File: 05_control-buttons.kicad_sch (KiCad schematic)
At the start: 8 parts, among them SW1 SW_Push, SW2 SW_Push, SW3 SW_Push, SW4 SW_Push

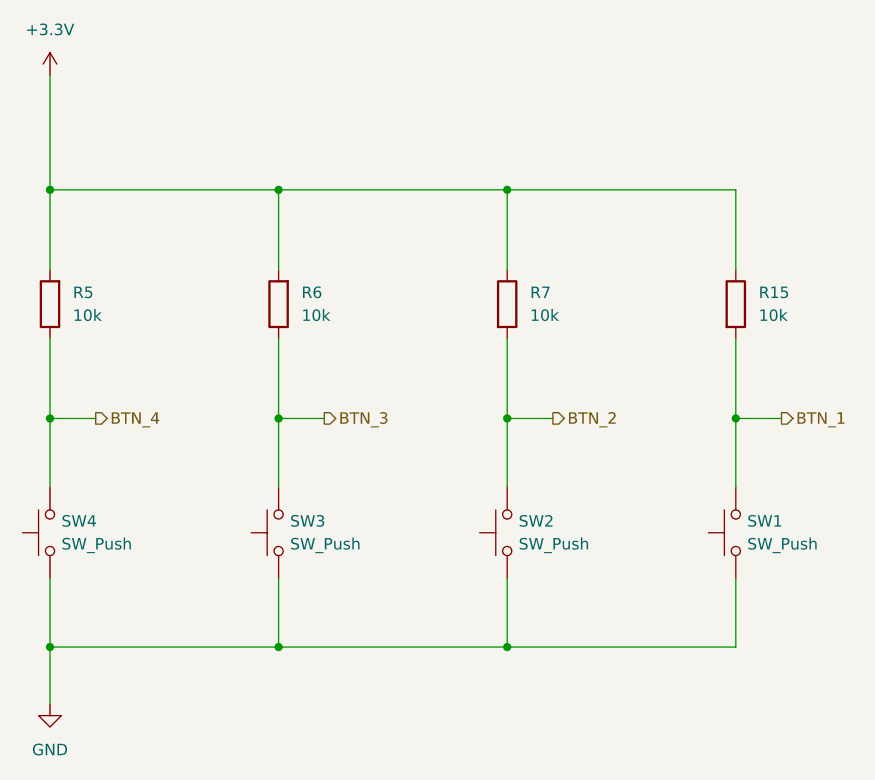
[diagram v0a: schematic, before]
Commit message: Reworked v2 routing
- some general improvements
- reworked component numbering
- routed and tuned differential pair (USB)
- added stiching vias and improved ground fills
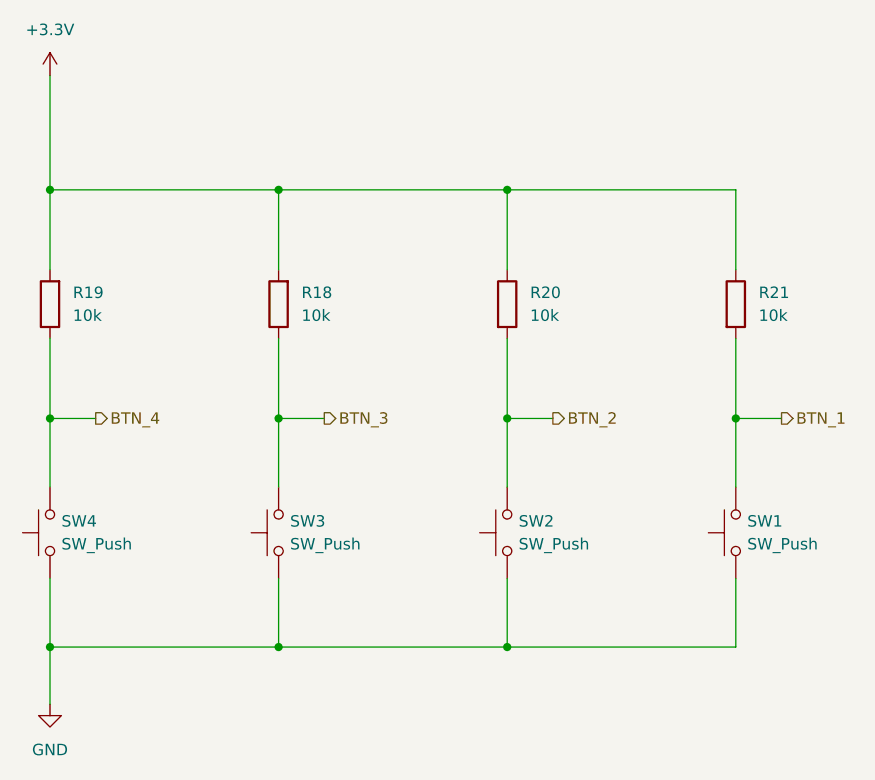
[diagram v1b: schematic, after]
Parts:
- renumbered R6 to R18, R5 to R19, R7 to R20, R15 to R21
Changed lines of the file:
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@@
 		(dnp no)
 		(fields_autoplaced yes)
-		(property "Reference" "R6"
+		(property "Reference" "R18"
 			(at 104.14 74.9299 0)
 			(effects
@@
 			(project "ZEReader-Pico"
 				(path "/ec954637-2a8b-4662-b4a1-f88107f11cb0/33ac9274-8ec9-4374-b845-560e6893b431"
-					(reference "R6")
+					(reference "R18")
 					(unit 1)
 				)
@@
 		(dnp no)
 		(fields_autoplaced yes)
-		(property "Reference" "R15"
+		(property "Reference" "R21"
 			(at 154.94 74.9299 0)
 			(effects
@@
 			(project "ZEReader-Pico"
 				(path "/ec954637-2a8b-4662-b4a1-f88107f11cb0/33ac9274-8ec9-4374-b845-560e6893b431"
-					(reference "R15")
+					(reference "R21")
 					(unit 1)
 				)
@@
 		(dnp no)
 		(fields_autoplaced yes)
-		(property "Reference" "R5"
+		(property "Reference" "R19"
 			(at 78.74 74.9299 0)
 			(effects
@@
 			(project ""
 				(path "/ec954637-2a8b-4662-b4a1-f88107f11cb0/33ac9274-8ec9-4374-b845-560e6893b431"
-					(reference "R5")
+					(reference "R19")
 					(unit 1)
 				)
@@
 		(dnp no)
 		(fields_autoplaced yes)
-		(property "Reference" "R7"
+		(property "Reference" "R20"
 			(at 129.54 74.9299 0)
 			(effects
@@
 			(project "ZEReader-Pico"
 				(path "/ec954637-2a8b-4662-b4a1-f88107f11cb0/33ac9274-8ec9-4374-b845-560e6893b431"
-					(reference "R7")
-					(unit 1)
-				)
+					(reference "R20")
+					(unit 1)
+				)

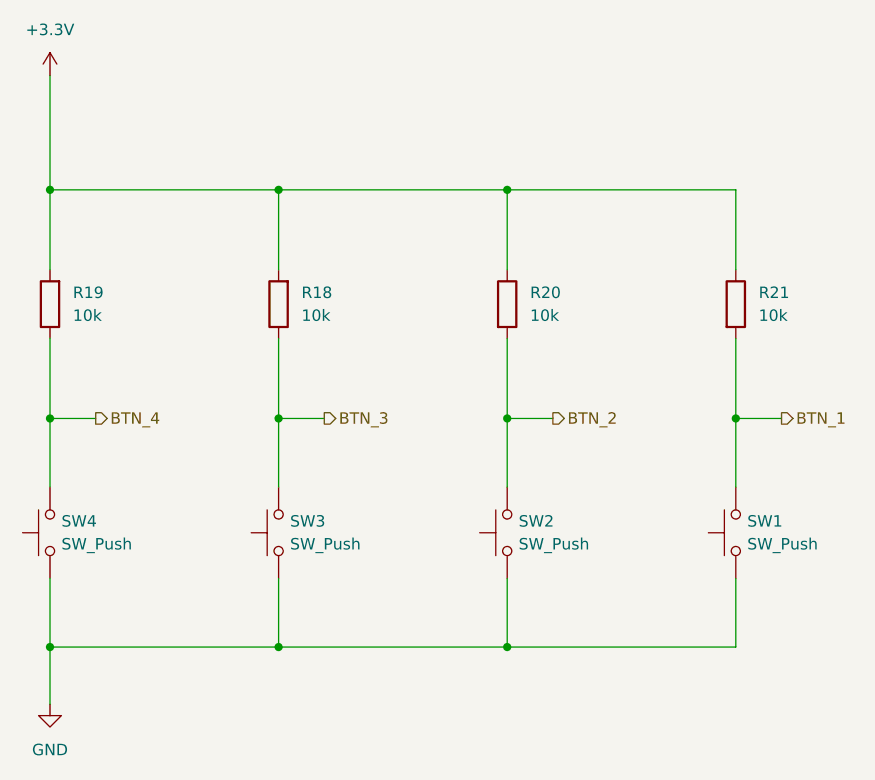
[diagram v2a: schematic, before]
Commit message: Connect both USB data lines again, checked everything with datasheets again
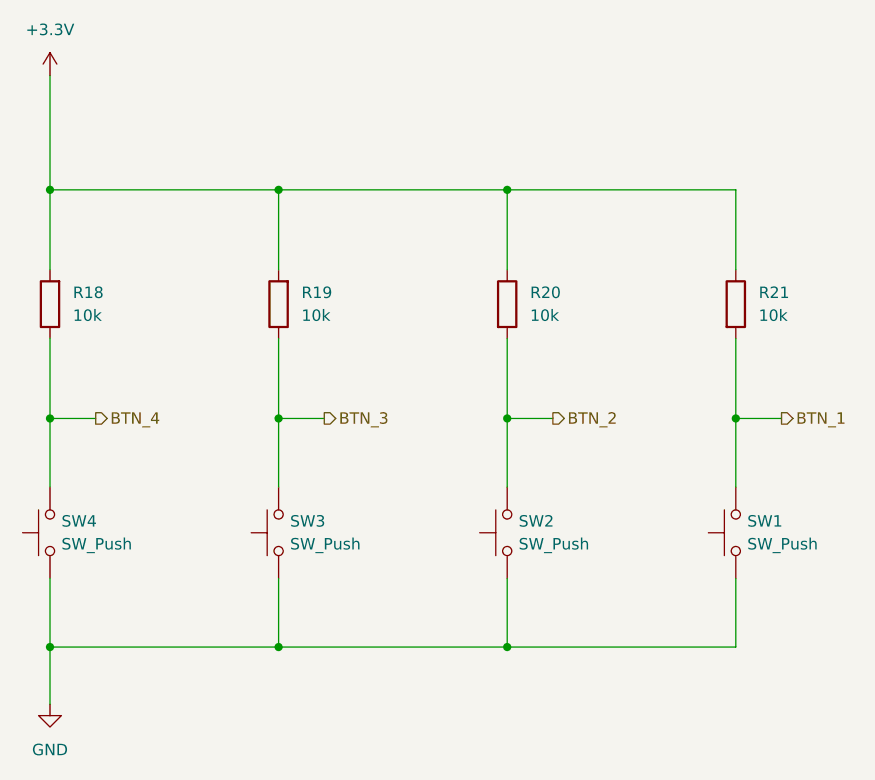
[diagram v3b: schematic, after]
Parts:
- renumbered R19 to R18, R18 to R19
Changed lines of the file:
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@@
 		(dnp no)
 		(fields_autoplaced yes)
-		(property "Reference" "R18"
+		(property "Reference" "R19"
 			(at 104.14 74.9299 0)
 			(effects
@@
 			(project "ZEReader-Pico"
 				(path "/ec954637-2a8b-4662-b4a1-f88107f11cb0/33ac9274-8ec9-4374-b845-560e6893b431"
-					(reference "R18")
+					(reference "R19")
 					(unit 1)
 				)
@@
 		(dnp no)
 		(fields_autoplaced yes)
-		(property "Reference" "#PWR05"
+		(property "Reference" "#PWR029"
 			(at 76.2 54.61 0)
 			(effects
@@
 			(project ""
 				(path "/ec954637-2a8b-4662-b4a1-f88107f11cb0/33ac9274-8ec9-4374-b845-560e6893b431"
-					(reference "#PWR05")
+					(reference "#PWR029")
 					(unit 1)
 				)
@@
 		(dnp no)
 		(fields_autoplaced yes)
-		(property "Reference" "R19"
+		(property "Reference" "R18"
 			(at 78.74 74.9299 0)
 			(effects
@@
 			(project ""
 				(path "/ec954637-2a8b-4662-b4a1-f88107f11cb0/33ac9274-8ec9-4374-b845-560e6893b431"
-					(reference "R19")
+					(reference "R18")
 					(unit 1)
 				)
@@
 		(dnp no)
 		(fields_autoplaced yes)
-		(property "Reference" "#PWR06"
+		(property "Reference" "#PWR030"
 			(at 76.2 127 0)
 			(effects
@@
 			(project ""
 				(path "/ec954637-2a8b-4662-b4a1-f88107f11cb0/33ac9274-8ec9-4374-b845-560e6893b431"
-					(reference "#PWR06")
-					(unit 1)
-				)
+					(reference "#PWR030")
+					(unit 1)
+				)

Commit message: Bigger Zener, improved BoM, general improvements
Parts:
- R18, R19, R20, R21: DigiKey (none) -> 311-10.0KFRCT-ND; Manufacturer PartNo (none) -> RC1206FR-0710KL
- SW1, SW2, SW3, SW4: DigiKey (none) -> 450-1650-ND; Manufacturer PartNo (none) -> 1825910-6
